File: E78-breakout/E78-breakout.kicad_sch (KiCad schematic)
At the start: 17 parts, among them J1 Conn_01x04, J2 Conn_01x06, J3 Conn_01x04, J4 Conn_01x03, U1 E78, U2 AMS1117CS-3.3

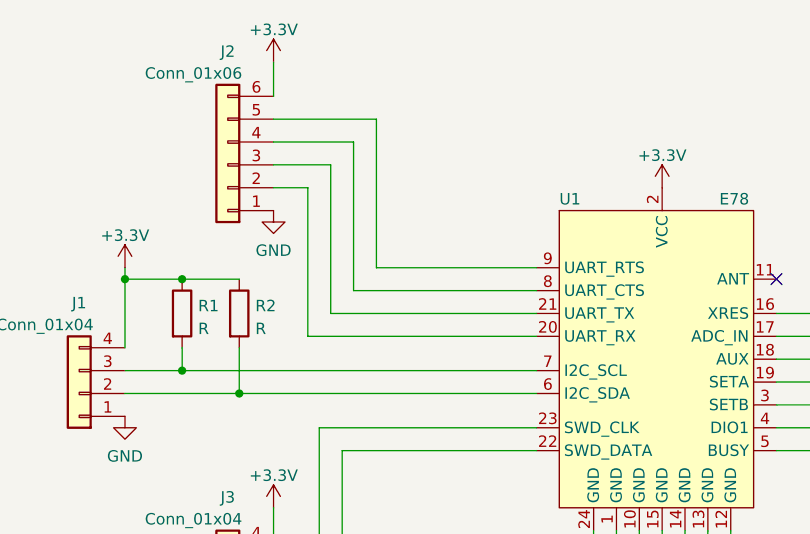
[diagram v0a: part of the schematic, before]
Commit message: routed e78 breakout
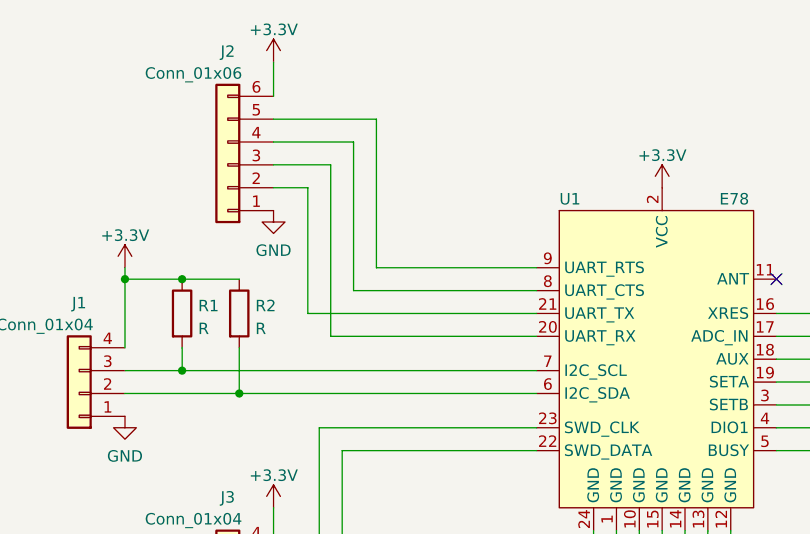
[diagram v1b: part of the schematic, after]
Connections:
- net at J2.2 (Pin_2): now also U1.21 (UART_TX); no longer U1.20 (UART_RX)
- net at J2.3 (Pin_3): now also U1.20 (UART_RX); no longer U1.21 (UART_TX)
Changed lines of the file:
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@@
   )
   (no_connect (at 154.94 77.47))
-  (wire (pts (xy 105.41 81.28) (xy 128.27 81.28))
+  (wire (pts (xy 128.27 83.82) (xy 105.41 83.82))
     (stroke (width 0) (type default))
   )
@@
   )
   (wire (pts (xy 82.55 77.47) (xy 88.9 77.47))
+    (stroke (width 0) (type default))
+  )
+  (wire (pts (xy 105.41 64.77) (xy 99.06 64.77))
+    (stroke (width 0) (type default))
+  )
+  (wire (pts (xy 105.41 83.82) (xy 105.41 64.77))
     (stroke (width 0) (type default))
   )
@@
     (stroke (width 0) (type default))
   )
-  (wire (pts (xy 102.87 83.82) (xy 102.87 67.31))
-    (stroke (width 0) (type default))
-  )
-  (wire (pts (xy 99.06 64.77) (xy 105.41 64.77))
-    (stroke (width 0) (type default))
-  )
   (wire (pts (xy 102.87 67.31) (xy 99.06 67.31))
     (stroke (width 0) (type default))
@@
     (stroke (width 0) (type default))
   )
+  (wire (pts (xy 102.87 67.31) (xy 102.87 81.28))
+    (stroke (width 0) (type default))
+  )
   (wire (pts (xy 194.31 85.09) (xy 189.23 85.09))
     (stroke (width 0) (type default))
   )
   (wire (pts (xy 95.25 90.17) (xy 128.27 90.17))
-    (stroke (width 0) (type default))
-  )
-  (wire (pts (xy 128.27 83.82) (xy 102.87 83.82))
     (stroke (width 0) (type default))
   )
@@
   )
   (wire (pts (xy 147.32 109.22) (xy 149.86 109.22))
-    (stroke (width 0) (type default))
-  )
-  (wire (pts (xy 105.41 64.77) (xy 105.41 81.28))
     (stroke (width 0) (type default))
   )
@@
     (stroke (width 0) (type default))
   )
+  (wire (pts (xy 102.87 81.28) (xy 128.27 81.28))
+    (stroke (width 0) (type default))
+  )
